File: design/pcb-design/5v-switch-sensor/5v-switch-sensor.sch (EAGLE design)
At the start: 20 parts, among them U2 ATMEGA328P_PDIP

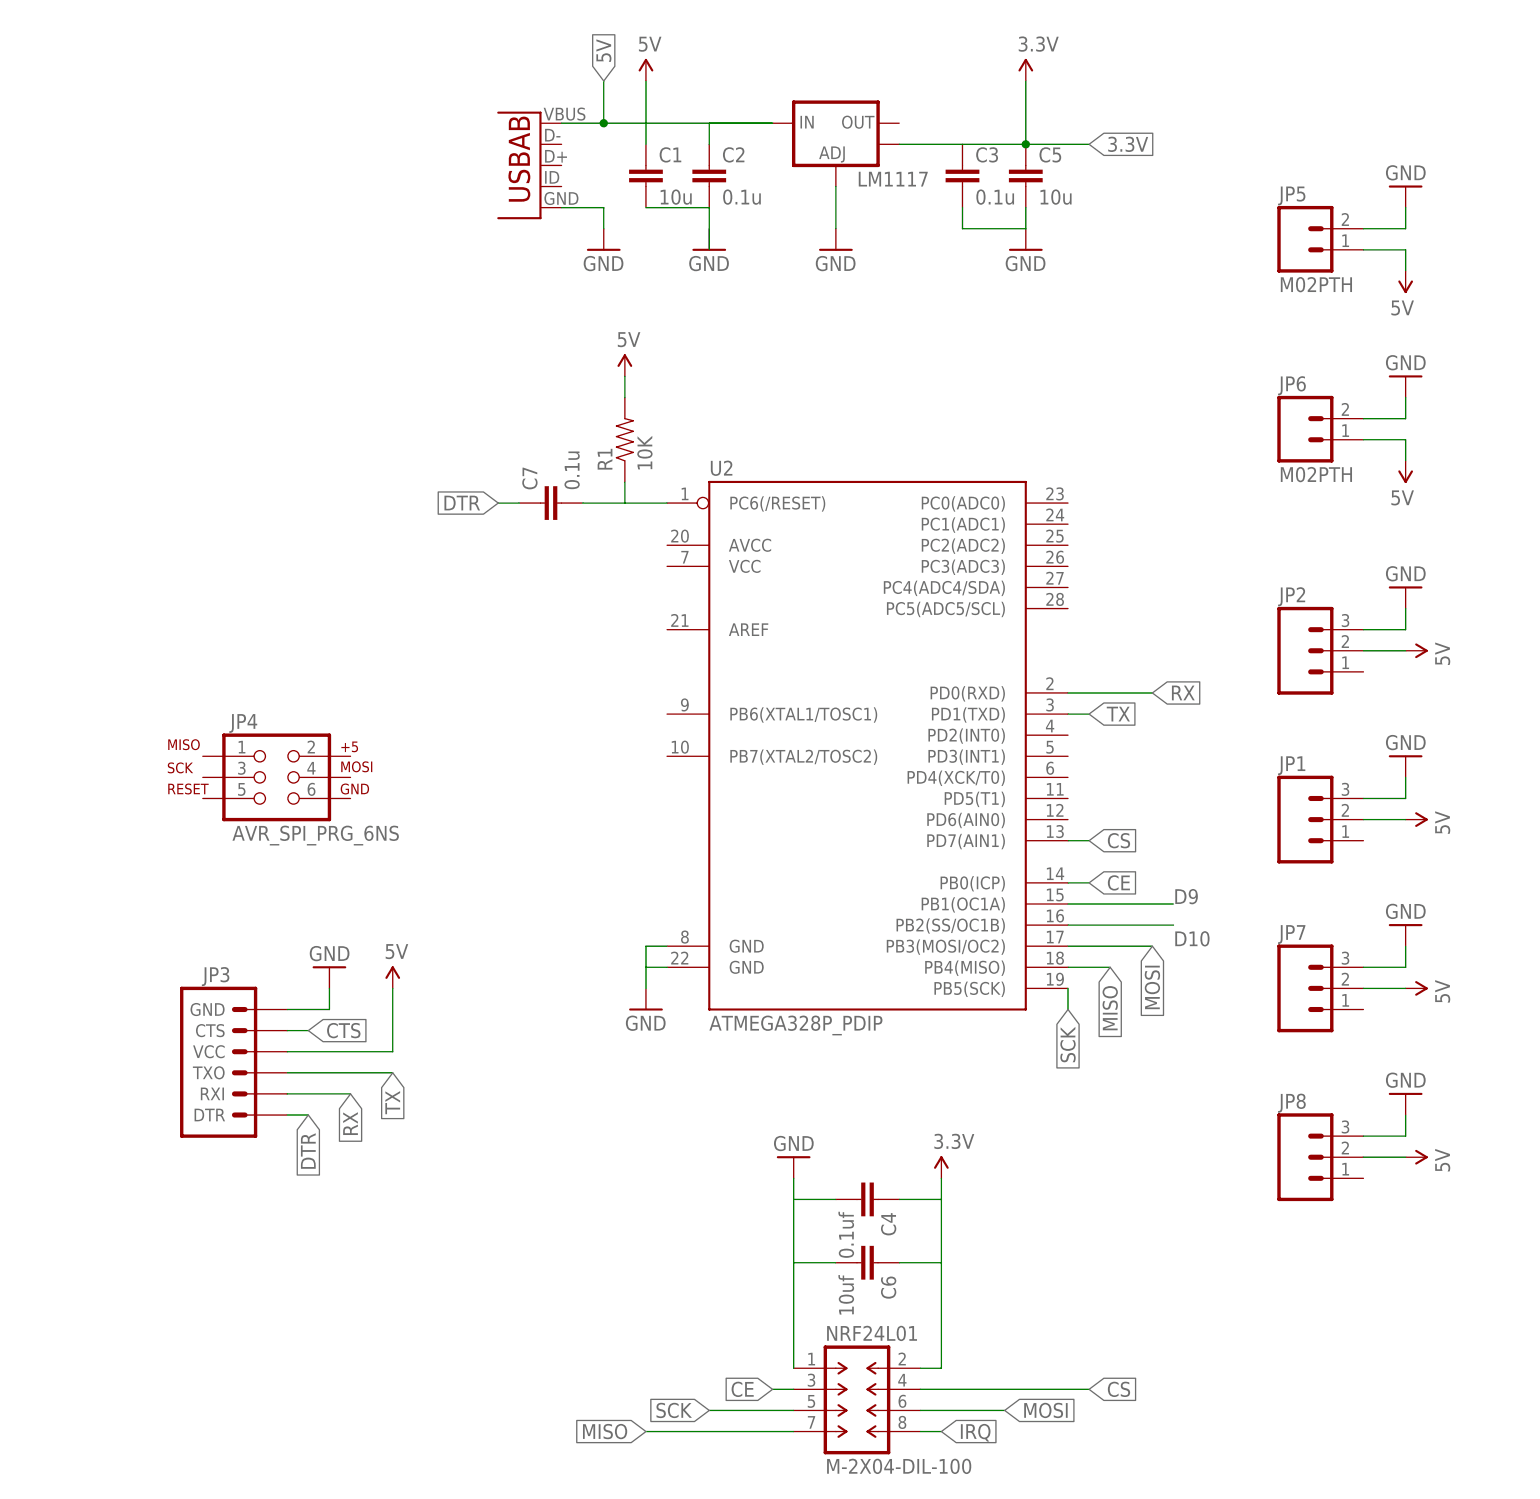
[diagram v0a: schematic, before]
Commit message: pcb-design: new board file for 5v-switch-sensor and fixes for sch file.
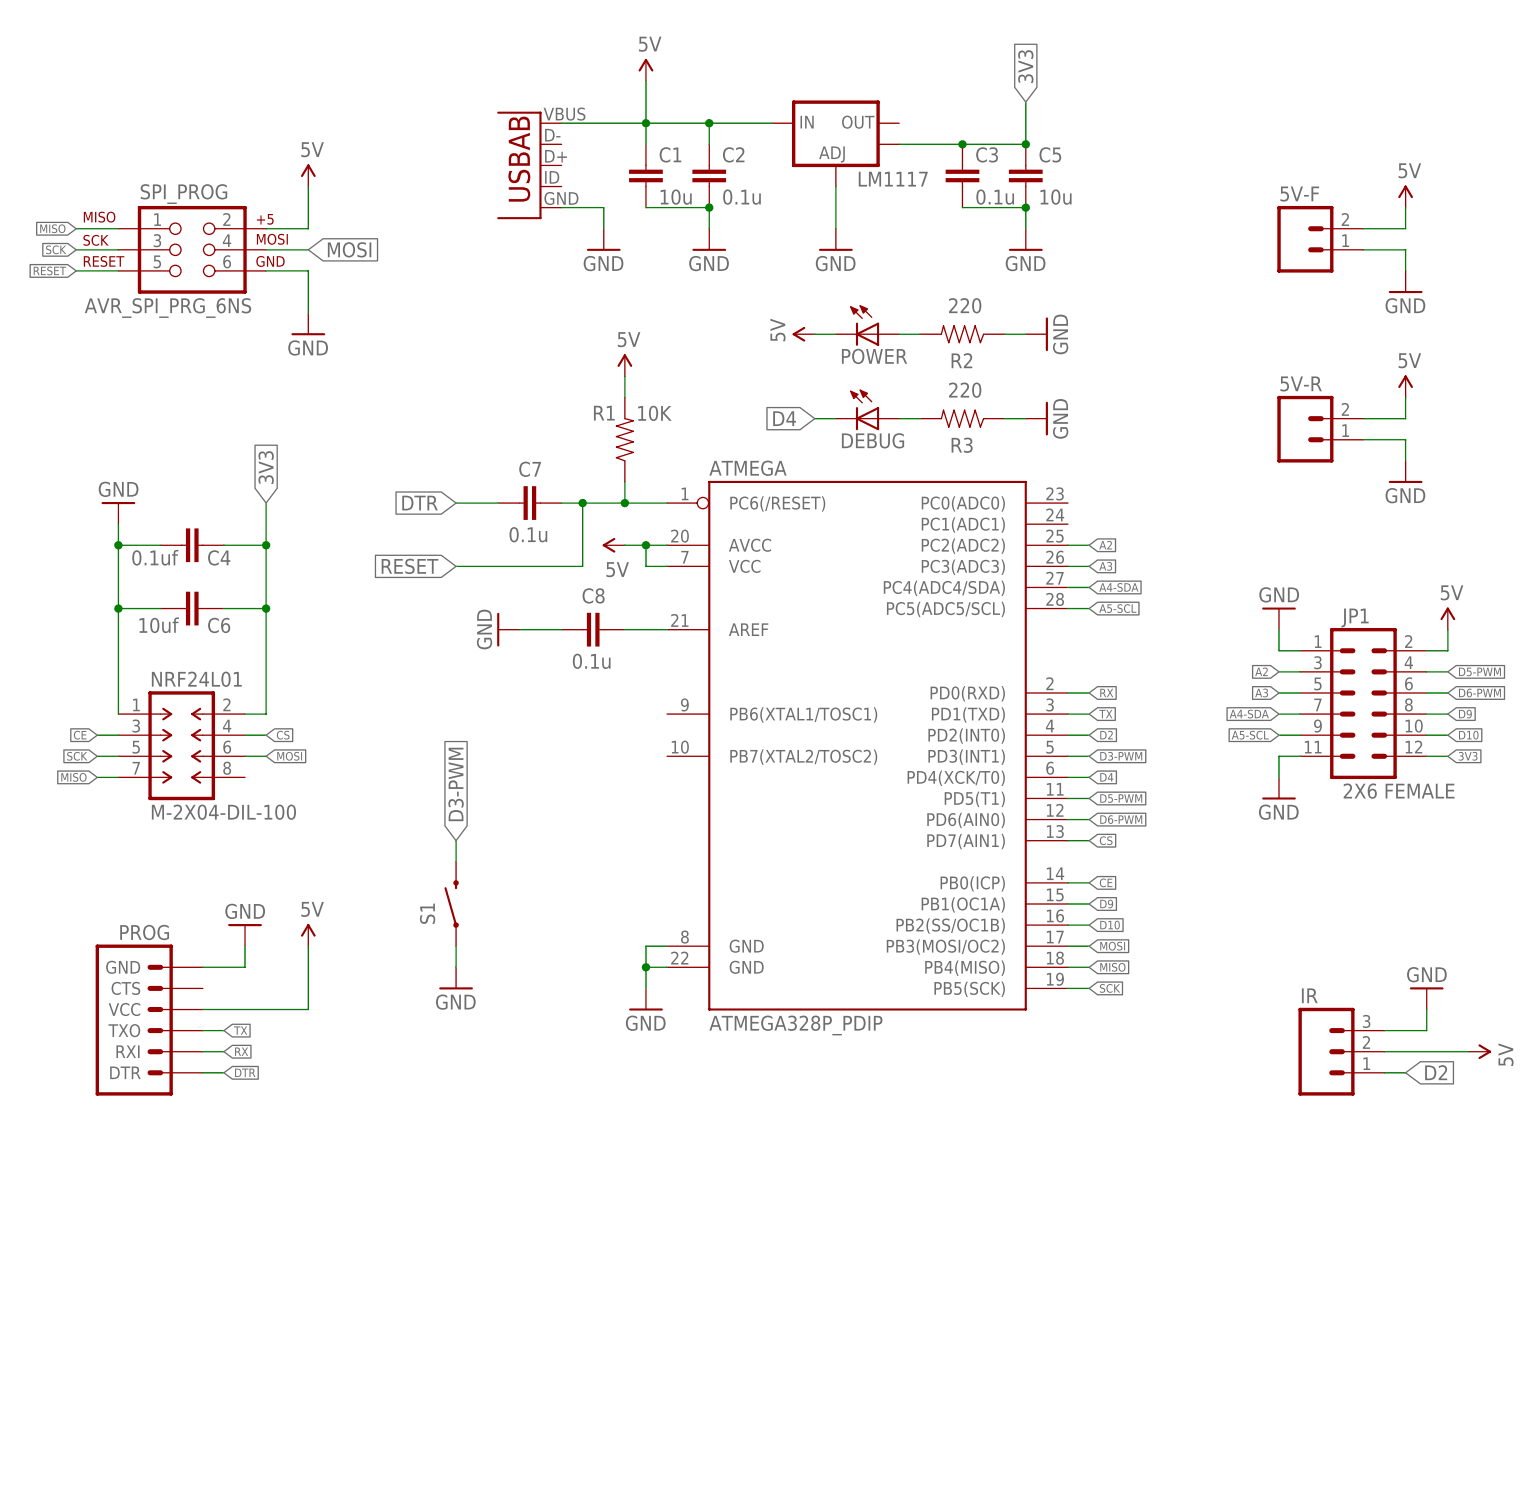
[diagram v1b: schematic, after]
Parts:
- removed JP2, JP7, JP8: (no value), SparkFun-Connectors:M03PTH
- removed JP3: (no value), SparkFun-Connectors:ARDUINO_SERIAL_PROGRAMPTH
- removed JP4: AVR_SPI_PRG_6NS, SparkFun-Connectors:AVR_SPI_PRG_6NS
- added C8: 0.1u, SparkFun-Capacitors:CAP0805
- added DEBUG, POWER: (no value), adafruit:LEDCHIPLED_0805
- added IR: (no value), SparkFun-Connectors:M03PTH
- added PROG: (no value), SparkFun-Connectors:ARDUINO_SERIAL_PROGRAMPTH
- added R2, R3: 220, SparkFun-Resistors:RESISTOR0805-RES
- added S1: SWITCH-MOMENTARY-2SMD-1101NE, SparkFun-Electromechanical:SWITCH-MOMENTARY-2SMD-1101NE
- added SPI_PROG: AVR_SPI_PRG_6NS, SparkFun-Connectors:AVR_SPI_PRG_6NS
- JP1: value (none) -> 2X6 FEMALE; device SparkFun-Connectors:M03PTH -> SparkFun-Connectors:M06X2PTH_FEMALE
- renumbered JP5 to 5V-F, JP6 to 5V-R, U2 to ATMEGA
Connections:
- removed net 3.3V: C3.1, C4.1, C5.1, C6.1, LM1117.OUT@1, NRF24L01.2
- removed net CTS: JP3.CTS
- removed net IRQ: NRF24L01.8
- removed net N$1: C1.2, C2.2
- new net 3V3: C3.1, C4.1, C5.1, C6.1, JP1.12, LM1117.OUT@1, NRF24L01.2
- new net A2: ATMEGA.PC2(ADC2), JP1.3
- new net A3: ATMEGA.PC3(ADC3), JP1.5
- new net A4-SDA: ATMEGA.PC4(ADC4/SDA), JP1.7
- new net A5-SCL: ATMEGA.PC5(ADC5/SCL), JP1.9
- new net D2: ATMEGA.PD2(INT0), IR.1
- new net D3-PWM: ATMEGA.PD3(INT1), S1.2
- new net D4: ATMEGA.PD4(XCK/T0), DEBUG.C
- new net D5-PWM: ATMEGA.PD5(T1), JP1.4
- new net D6-PWM: ATMEGA.PD6(AIN0), JP1.6
- new net N$3: ATMEGA.AREF, C8.2
- new net N$4: DEBUG.A, R3.2
- new net RESET: ATMEGA.PC6(/RESET), C7.2, R1.1, SPI_PROG.5
- net 5V: now also 5V-F.2, 5V-R.2, ATMEGA.AVCC, ATMEGA.VCC, IR.2, POWER.C, PROG.VCC, SPI_PROG.2; no longer 5V-F.1, 5V-R.1, JP2.2, JP3.VCC, JP7.2, JP8.2
- net D10: now also JP1.10
- net D9: now also JP1.8
- net DTR: now also PROG.DTR; no longer JP3.DTR
- net GND: now also 5V-F.1, 5V-R.1, C1.2, C2.2, C8.1, IR.3, JP1.1, JP1.11, PROG.GND, R2.1, R3.1, S1.1, SPI_PROG.6; no longer 5V-F.2, 5V-R.2, JP1.3, JP2.3, JP3.GND, JP7.3, JP8.3
- net MISO: now also SPI_PROG.1
- net MOSI: now also SPI_PROG.4
- net N$2: now also POWER.A, R2.2; no longer ATMEGA.PC6(/RESET), C7.2, R1.1
- net RX: now also PROG.RXI; no longer JP3.RXI
- net SCK: now also SPI_PROG.3
- net TX: now also PROG.TXO; no longer JP3.TXO
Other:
- moved on the sheet: C4, C6, C7, NRF24L01

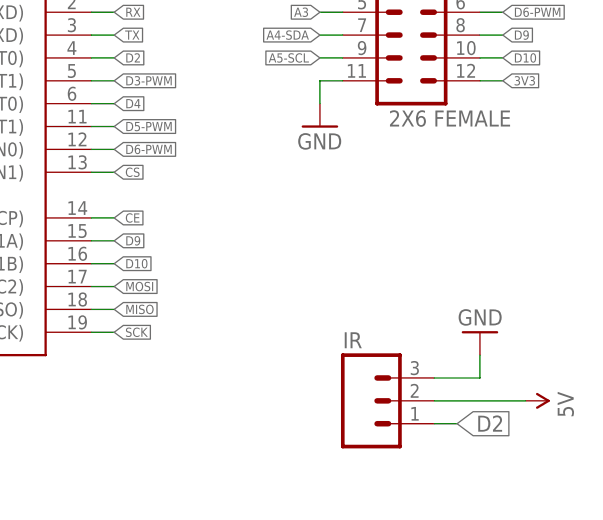
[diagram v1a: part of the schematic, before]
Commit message: pcb-design: [5v-switch-sensor] added noise reduction to IR circuit
Signed-off-by: Kiveisha Yevgeniy <lodmilak@gmail.com>
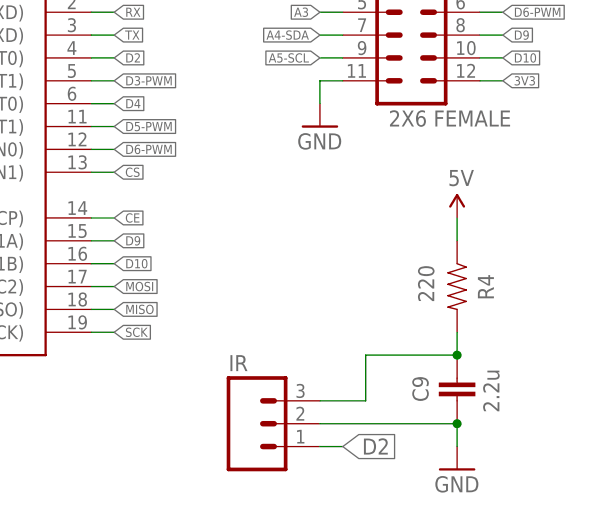
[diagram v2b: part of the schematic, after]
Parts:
- added C9: 2.2u, SparkFun-Capacitors:CAP0805
- added R4: 220, SparkFun-Resistors:RESISTOR0805-RES
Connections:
- new net N$1: C9.2, IR.3, R4.2
- net 5V: now also R4.1; no longer IR.2
- net GND: now also C9.1, IR.2; no longer IR.3
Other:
- moved on the sheet: IR
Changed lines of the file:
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@@
 <?xml version="1.0" encoding="utf-8"?>
 <!DOCTYPE eagle SYSTEM "eagle.dtd">
-<eagle version="7.1.0">
+<eagle version="7.2.0">
 <drawing>
 <settings>
@@
 <part name="GND10" library="SparkFun-Aesthetics" deviceset="GND" device=""/>
 <part name="GND17" library="SparkFun-Aesthetics" deviceset="GND" device=""/>
+<part name="R4" library="SparkFun-Resistors" deviceset="RESISTOR" device="0805-RES" value="220"/>
+<part name="C9" library="SparkFun-Capacitors" deviceset="CAP" device="0805" value="2.2u"/>
 </parts>
 <sheets>
@@
 <instance part="SUPPLY7" gate="G$1" x="25.4" y="78.74"/>
 <instance part="GND9" gate="1" x="27.94" y="2.54"/>
-<instance part="IR" gate="G$1" x="109.22" y="-2.54"/>
-<instance part="SUPPLY11" gate="G$1" x="127" y="-2.54" rot="R270"/>
-<instance part="GND13" gate="1" x="121.92" y="5.08" rot="R180"/>
+<instance part="IR" gate="G$1" x="96.52" y="-5.08"/>
+<instance part="SUPPLY11" gate="G$1" x="119.38" y="17.78"/>
+<instance part="GND13" gate="1" x="119.38" y="-10.16"/>
 <instance part="SUPPLY4" gate="G$1" x="119.38" y="99.06"/>
 <instance part="SUPPLY5" gate="G$1" x="119.38" y="76.2"/>
@@
 <instance part="GND10" gate="1" x="104.14" y="50.8" rot="R180"/>
 <instance part="GND17" gate="1" x="104.14" y="27.94"/>
+<instance part="R4" gate="G$1" x="119.38" y="10.16" smashed="yes" rot="R270">
+<attribute name="NAME" x="123.4694" y="8.636" size="1.778" layer="95" rot="R90"/>
+<attribute name="VALUE" x="116.84" y="8.382" size="1.778" layer="96" rot="R90"/>
+</instance>
+<instance part="C9" gate="G$1" x="119.38" y="0" smashed="yes" rot="R180">
+<attribute name="NAME" x="114.427" y="0.254" size="1.778" layer="95" rot="R270"/>
+<attribute name="VALUE" x="122.301" y="1.016" size="1.778" layer="96" rot="R270"/>
+</instance>
 </instances>
 <busses>
@@
 </segment>
 <segment>
-<pinref part="IR" gate="G$1" pin="3"/>
-<pinref part="GND13" gate="1" pin="GND"/>
-<wire x1="116.84" y1="0" x2="121.92" y2="0" width="0.1524" layer="91"/>
-<wire x1="121.92" y1="0" x2="121.92" y2="2.54" width="0.1524" layer="91"/>
-</segment>
-<segment>
 <pinref part="5V-F" gate="G$1" pin="1"/>
 <pinref part="GND7" gate="1" pin="GND"/>
@@
 <wire x1="106.68" y1="33.02" x2="104.14" y2="33.02" width="0.1524" layer="91"/>
 <wire x1="104.14" y1="33.02" x2="104.14" y2="30.48" width="0.1524" layer="91"/>
+</segment>
+<segment>
+<pinref part="C9" gate="G$1" pin="1"/>
+<pinref part="GND13" gate="1" pin="GND"/>
+<wire x1="119.38" y1="-5.08" x2="119.38" y2="-7.62" width="0.1524" layer="91"/>
+<pinref part="IR" gate="G$1" pin="2"/>
+<wire x1="104.14" y1="-5.08" x2="119.38" y2="-5.08" width="0.1524" layer="91"/>
+<junction x="119.38" y="-5.08"/>
 </segment>
 </net>
@@
 </segment>
 <segment>
-<pinref part="IR" gate="G$1" pin="2"/>
-<pinref part="SUPPLY11" gate="G$1" pin="5V"/>
-<wire x1="116.84" y1="-2.54" x2="127" y2="-2.54" width="0.1524" layer="91"/>
-</segment>
-<segment>
 <pinref part="5V-F" gate="G$1" pin="2"/>
 <pinref part="SUPPLY4" gate="G$1" pin="5V"/>
@@
 <wire x1="121.92" y1="45.72" x2="124.46" y2="45.72" width="0.1524" layer="91"/>
 <wire x1="124.46" y1="45.72" x2="124.46" y2="48.26" width="0.1524" layer="91"/>
+</segment>
+<segment>
+<pinref part="SUPPLY11" gate="G$1" pin="5V"/>
+<pinref part="R4" gate="G$1" pin="1"/>
+<wire x1="119.38" y1="17.78" x2="119.38" y2="15.24" width="0.1524" layer="91"/>
 </segment>
 </net>
@@
 <segment>
 <pinref part="IR" gate="G$1" pin="1"/>
-<wire x1="116.84" y1="-5.08" x2="119.38" y2="-5.08" width="0.1524" layer="91"/>
-<label x="119.38" y="-5.08" size="1.778" layer="95" xref="yes"/>
+<wire x1="104.14" y1="-7.62" x2="106.68" y2="-7.62" width="0.1524" layer="91"/>
+<label x="106.68" y="-7.62" size="1.778" layer="95" xref="yes"/>
 </segment>
 </net>
@@
 </segment>
 </net>
+<net name="N$1" class="0">
+<segment>
+<pinref part="R4" gate="G$1" pin="2"/>
+<pinref part="C9" gate="G$1" pin="2"/>
+<wire x1="119.38" y1="5.08" x2="119.38" y2="2.54" width="0.1524" layer="91"/>
+<pinref part="IR" gate="G$1" pin="3"/>
+<wire x1="104.14" y1="-2.54" x2="109.22" y2="-2.54" width="0.1524" layer="91"/>
+<wire x1="109.22" y1="-2.54" x2="109.22" y2="2.54" width="0.1524" layer="91"/>
+<wire x1="119.38" y1="2.54" x2="109.22" y2="2.54" width="0.1524" layer="91"/>
+<junction x="119.38" y="2.54"/>
+</segment>
+</net>

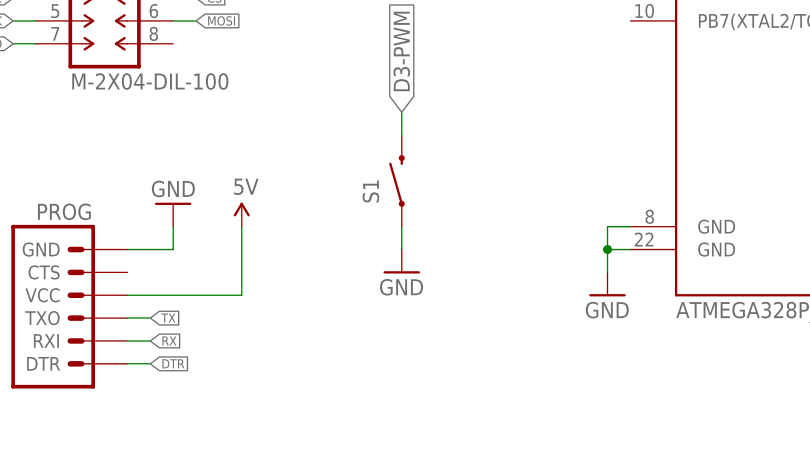
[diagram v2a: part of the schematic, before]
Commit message: pcb-design: 5v pcb fixes before sendinf to imall and start of 3v pcb
Signed-off-by: Kiveisha Yevgeniy <lodmilak@gmail.com>
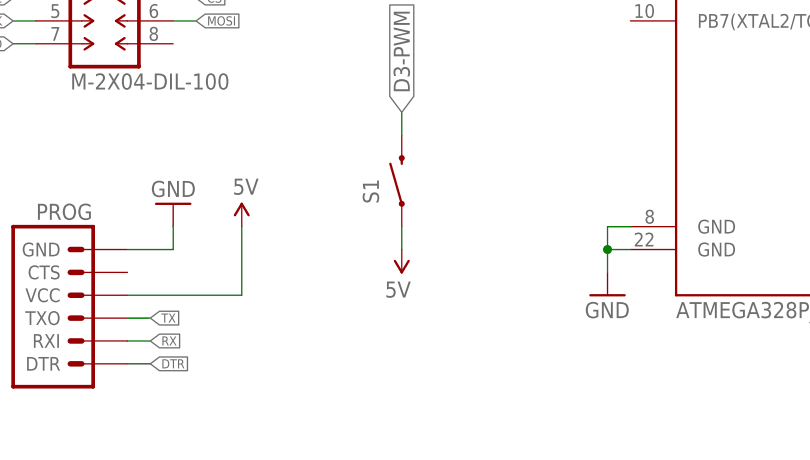
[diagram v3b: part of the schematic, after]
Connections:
- net 5V: now also S1.1
- net GND: no longer S1.1
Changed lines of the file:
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@@
 <part name="GND15" library="SparkFun-Aesthetics" deviceset="GND" device=""/>
 <part name="S1" library="SparkFun-Electromechanical" deviceset="SWITCH-MOMENTARY-2" device="SMD-1101NE"/>
-<part name="GND16" library="SparkFun-Aesthetics" deviceset="GND" device=""/>
 <part name="JP1" library="SparkFun-Connectors" deviceset="M06X2" device="PTH_FEMALE" value="2X6 FEMALE"/>
 <part name="SUPPLY2" library="SparkFun-Aesthetics" deviceset="5V" device=""/>
@@
 <part name="R4" library="SparkFun-Resistors" deviceset="RESISTOR" device="0805-RES" value="220"/>
 <part name="C9" library="SparkFun-Capacitors" deviceset="CAP" device="0805" value="2.2u"/>
+<part name="SUPPLY3" library="SparkFun-Aesthetics" deviceset="5V" device=""/>
 </parts>
 <sheets>
@@
 <attribute name="NAME" x="2.54" y="12.7" size="1.778" layer="95" rot="R90"/>
 </instance>
-<instance part="GND16" gate="1" x="5.08" y="5.08"/>
 <instance part="JP1" gate="G$1" x="111.76" y="33.02"/>
 <instance part="SUPPLY2" gate="G$1" x="124.46" y="48.26"/>
@@
 <attribute name="VALUE" x="122.301" y="1.016" size="1.778" layer="96" rot="R270"/>
 </instance>
+<instance part="SUPPLY3" gate="G$1" x="5.08" y="7.62" rot="R180"/>
 </instances>
 <busses>
@@
 <pinref part="GND15" gate="1" pin="GND"/>
 <wire x1="71.12" y1="73.66" x2="73.66" y2="73.66" width="0.1524" layer="91"/>
-</segment>
-<segment>
-<pinref part="S1" gate="G$1" pin="1"/>
-<pinref part="GND16" gate="1" pin="GND"/>
-<wire x1="5.08" y1="10.16" x2="5.08" y2="7.62" width="0.1524" layer="91"/>
 </segment>
 <segment>
@@
 <wire x1="119.38" y1="17.78" x2="119.38" y2="15.24" width="0.1524" layer="91"/>
 </segment>
+<segment>
+<pinref part="S1" gate="G$1" pin="1"/>
+<pinref part="SUPPLY3" gate="G$1" pin="5V"/>
+<wire x1="5.08" y1="10.16" x2="5.08" y2="7.62" width="0.1524" layer="91"/>
+</segment>
 </net>
